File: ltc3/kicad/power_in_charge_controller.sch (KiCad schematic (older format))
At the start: 112 parts, among them P201 PV_IN, P202 LAB_IN, P203 S2BPHKS, Q201 BSC028N06NS, Q202 BSC028N06NS, Q203 BSC028N06NS, Q204 BSC028N06NS, Q205 ZVN4525E6, Q206 Q_PMOS_DGS, Q207 Q_NPN_BCE, U201 PI2127, U202 PI2127, U203 LTC2990, U204 LT8490

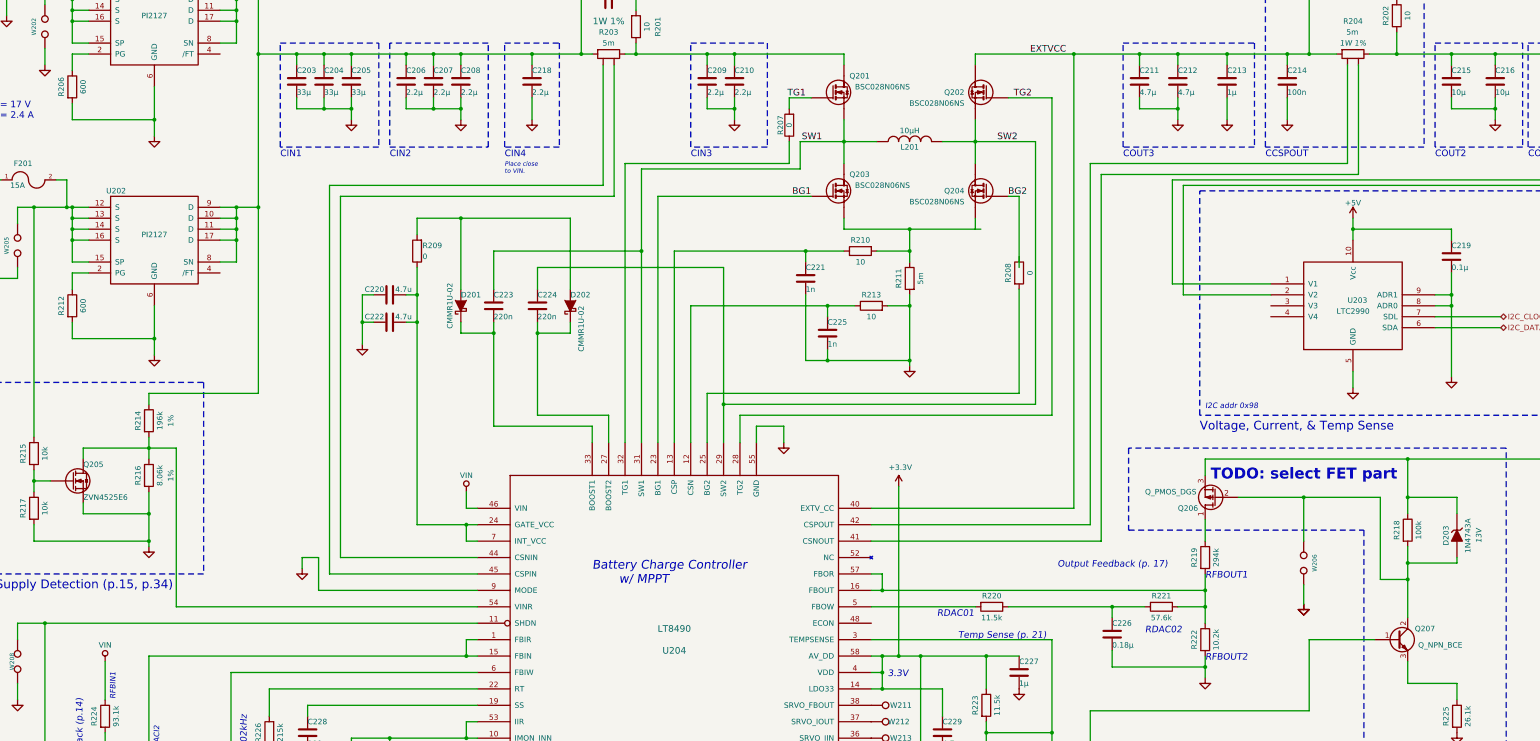
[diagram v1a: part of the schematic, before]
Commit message: LTC3: Minor Power Management Changes to LT8490
-replaced 600 ohm resistor on ideal diode with 0 ohm resistor
-selected transistors for feedback resistor disconnect subcircuit
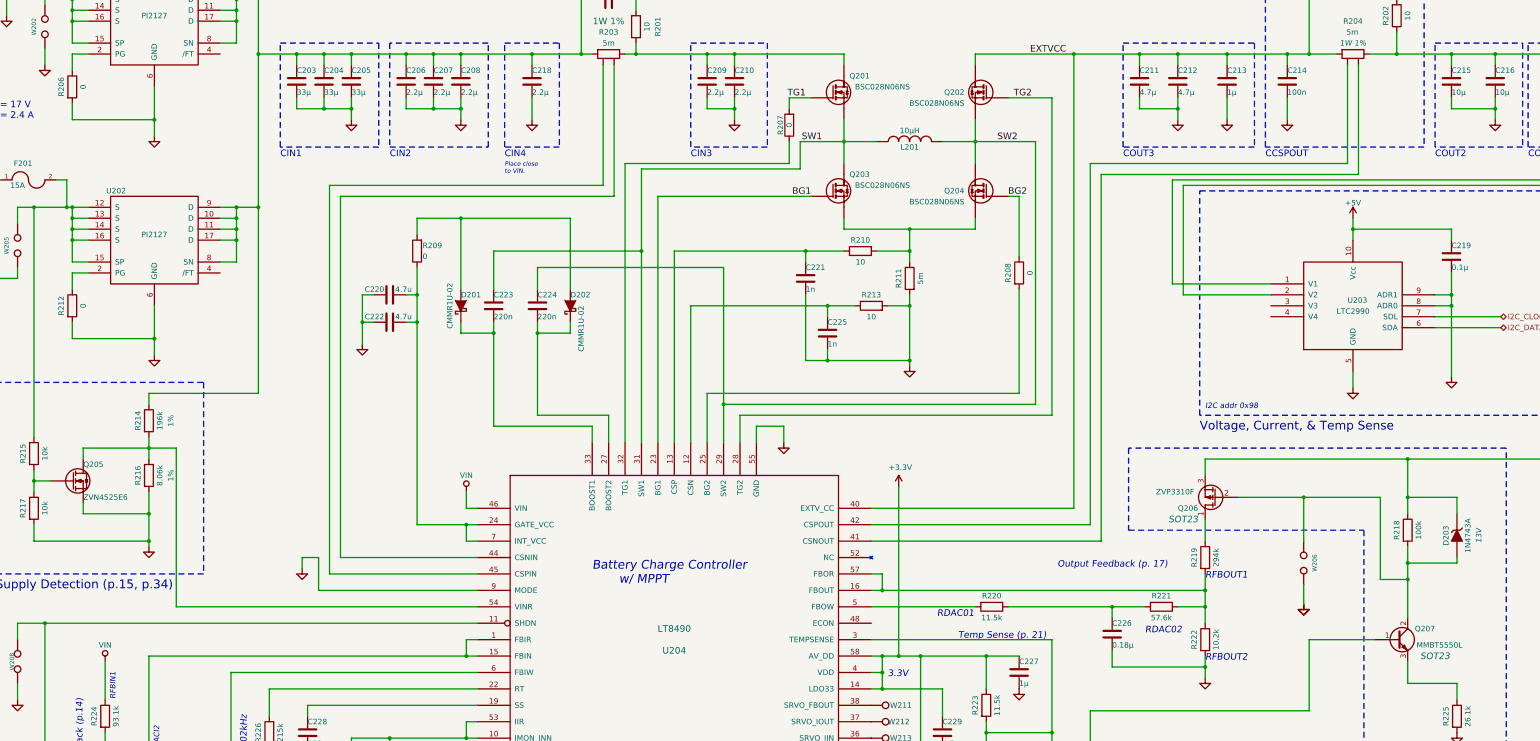
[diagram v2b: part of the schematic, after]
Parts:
- Q206: value Q_PMOS_DGS -> ZVP3310F; Package (none) -> SOT23
- Q207: value Q_NPN_BCE -> MMBT5550L; Package (none) -> SOT23
- R206, R212: value 600 -> 0
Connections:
- net BG2: now also R208.1
- net at Q203.3 (S), R210.2, R211.1: now also Q204.3 (S)
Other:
- note removed: "TODO: select FET part"
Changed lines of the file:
@@
 LIBS:atmel
 LIBS:audio
-LIBS:bbd
 LIBS:brooktre
 LIBS:cmos4000
@@
 LIBS:valves
 LIBS:video
-LIBS:Worldsemi
 LIBS:Xicor
 LIBS:xilinx
@@
 P 12200 5650
 F 0 "Q206" H 12550 5750 50  0000 R CNN
-F 1 "Q_PMOS_DGS" H 12850 5600 50  0000 R CNN
+F 1 "ZVP3310F" H 12750 5600 50  0000 R CNN
 F 2 "LTC3:PG-TDSON-8" H 12400 5750 29  0001 C CNN
 F 3 "" H 12200 5650 60  0000 C CNN
+F 4 "SOT23" H 12500 5850 60  0000 C CIN "Package"
 	1    12200 5650
 	-1   0    0    1
@@
 P 13850 6950
 F 0 "Q207" H 14200 7050 50  0000 R CNN
-F 1 "Q_NPN_BCE" H 14450 6900 50  0000 R CNN
+F 1 "MMBT5550L" H 14450 6900 50  0000 R CNN
 F 2 "TO_SOT_Packages_SMD:SOT-23" H 14050 7050 29  0001 C CNN
 F 3 "" H 13850 6950 60  0000 C CNN
+F 4 "SOT23" H 14200 6800 60  0000 C CIN "Package"
 	1    13850 6950
 	1    0    0    -1
@@
 P 1750 1900
 F 0 "R206" V 1650 1900 50  0000 C CNN
-F 1 "600" V 1850 1900 50  0000 C CNN
+F 1 "0" V 1850 1900 50  0000 C CNN
 F 2 "Resistors_SMD:R_0805" V 1680 1900 30  0001 C CNN
 F 3 "" H 1750 1900 30  0000 C CNN
@@
 P 1750 3900
 F 0 "R212" V 1650 3900 50  0000 C CNN
-F 1 "600" V 1850 3900 50  0000 C CNN
+F 1 "0" V 1850 3900 50  0000 C CNN
 F 2 "Resistors_SMD:R_0805" V 1680 3900 30  0001 C CNN
 F 3 "" H 1750 3900 30  0000 C CNN
@@
 SW2
 Wire Wire Line
-	8800 3200 10050 3200
+	8800 3200 10000 3200
 Wire Wire Line
 	10000 3200 10000 3100
@@
 Wire Wire Line
 	8000 5150 8000 5000
-Wire Wire Line
-	10400 2900 10400 3550
 Wire Wire Line
 	8300 2600 8300 2400
@@
 Wire Wire Line
 	3550 8050 3550 7950
-Text Notes 12150 5500 0    100  ~ 20
-TODO: select FET part
 $Comp
 L PI2127 U201
@@
 	1    0    0    -1
 $EndComp
+Wire Wire Line
+	10400 2900 10400 3450
 $EndSCHEMATC

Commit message: LTC3: Deleted "dummy" and "valve" footprint assignments.
The "dummy" footprints were meant for off-board components, but they
still found their way into the board layout as labels without any
pads, silkscreen, etc.

The "valve" footprints were meant as reminder placeholders of
components that still needed their final assignment.
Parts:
- P201, P202: footprint Valves:VALVE-OCTAL -> (none)
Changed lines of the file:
@@
 LIBS:transistors
 LIBS:ttl_ieee
-LIBS:valves
 LIBS:video
 LIBS:Xicor
@@
 F 0 "P201" H 800 900 50  0000 C CNN
 F 1 "PV_IN" V 900 1050 50  0000 C CNN
-F 2 "Valves:VALVE-OCTAL" H 800 1050 60  0001 C CNN
+F 2 "" H 800 1050 60  0001 C CNN
 F 3 "" H 800 1050 60  0000 C CNN
 	1    800  1050
@@
 F 0 "P202" H 800 2650 50  0000 C CNN
 F 1 "LAB_IN" V 900 2850 50  0000 C CNN
-F 2 "Valves:VALVE-OCTAL" H 800 2800 60  0001 C CNN
+F 2 "" H 800 2800 60  0001 C CNN
 F 3 "" H 800 2800 60  0000 C CNN
 	1    800  2800

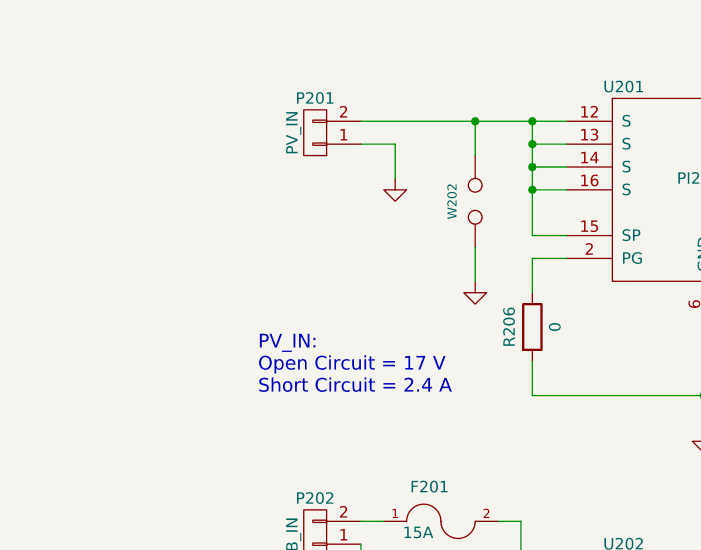
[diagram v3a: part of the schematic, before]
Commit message: LTC3: More footprint assignment.
Set footprint to "OFF-BOARD" for all off-board components.  This
results in an error dialog when opening the footprint assignment tool,
but it makes it obvious which components shouldn't have any footprint
assigned.
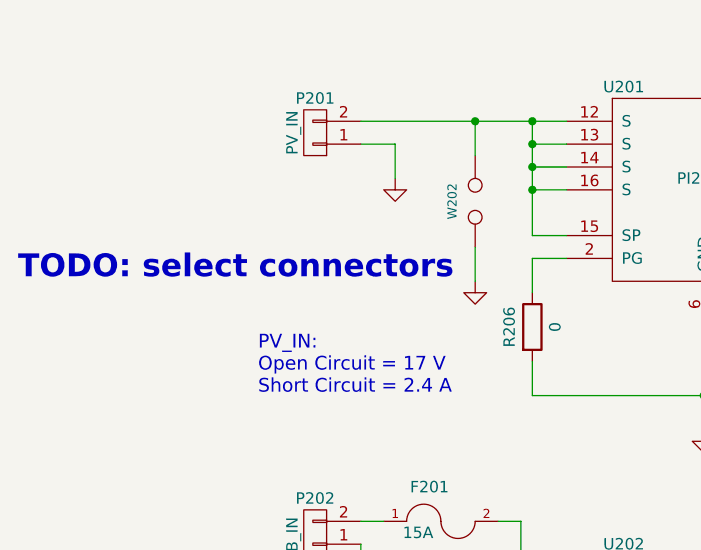
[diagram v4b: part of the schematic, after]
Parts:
- Q201, Q202, Q203, Q204: footprint SO-8 -> Power_Integrations:SO-8
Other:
- note added: "TODO: select connectors"
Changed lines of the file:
@@
 LIBS:atmel
 LIBS:audio
+LIBS:bbd
 LIBS:brooktre
 LIBS:cmos4000
@@
 LIBS:transistors
 LIBS:ttl_ieee
-LIBS:video
-LIBS:Xicor
-LIBS:xilinx
-LIBS:Zilog
 LIBS:Launch_Tower_Computer_III-cache
 EELAYER 25 0
@@
 F 0 "Q201" H 8850 2000 50  0000 L CNN
 F 1 "BSC028N06NS" H 8900 1900 50  0000 L CNN
-F 2 "SO-8" H 8950 1805 50  0001 L CNN
+F 2 "Power_Integrations:SO-8" H 8950 1805 50  0001 L CNN
 F 3 "" H 8700 1850 50  0000 L CNN
 	1    8500 1900
@@
 F 0 "Q202" H 10700 1850 50  0000 L CNN
 F 1 "BSC028N06NS" H 10700 1750 50  0000 L CNN
-F 2 "SO-8" H 10750 1805 50  0001 L CNN
+F 2 "Power_Integrations:SO-8" H 10750 1805 50  0001 L CNN
 F 3 "" H 10500 1850 50  0000 L CNN
 	1    10300 1900
@@
 F 0 "Q203" H 8850 2900 50  0000 L CNN
 F 1 "BSC028N06NS" H 8900 2800 50  0000 L CNN
-F 2 "SO-8" H 8950 2705 50  0001 L CNN
+F 2 "Power_Integrations:SO-8" H 8950 2705 50  0001 L CNN
 F 3 "" H 8700 2750 50  0000 L CNN
 	1    8500 2800
@@
 F 0 "Q204" H 10700 2750 50  0000 L CNN
 F 1 "BSC028N06NS" H 10700 2650 50  0000 L CNN
-F 2 "SO-8" H 10750 2705 50  0001 L CNN
+F 2 "Power_Integrations:SO-8" H 10750 2705 50  0001 L CNN
 F 3 "" H 10500 2750 50  0000 L CNN
 	1    10300 2800
@@
 F 0 "U201" H 2150 1750 50  0000 C CNN
 F 1 "PI2127" H 2500 1350 50  0000 C CNN
-F 2 "" H 2600 950 100 0000 C CNN
+F 2 "" H 2600 950 100 0001 C CNN
 F 3 "" H 2600 950 100 0000 C CNN
 	1    2500 1300
@@
 F 0 "U202" H 2150 3750 50  0000 C CNN
 F 1 "PI2127" H 2500 3350 50  0000 C CNN
-F 2 "" H 2600 2950 100 0000 C CNN
+F 2 "" H 2600 2950 100 0001 C CNN
 F 3 "" H 2600 2950 100 0000 C CNN
 	1    2500 3300
@@
 F 0 "Q205" H 1850 5650 50  0000 L CNN
 F 1 "ZVN4525E6" H 1850 5350 50  0000 L CNN
-F 2 "" H 1950 5600 50  0000 C CNN
+F 2 "" H 1950 5600 50  0001 C CNN
 F 3 "" H 1750 5500 50  0000 C CNN
 	1    1750 5500
@@
 Wire Wire Line
 	10400 2900 10400 3450
+Text Notes -500 1700 0    100  ~ 20
+TODO: select connectors
 $EndSCHEMATC
